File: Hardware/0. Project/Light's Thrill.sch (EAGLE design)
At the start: 26 parts, among them CN6 mini-PCIe board connector, U2 ATMEGA32U4, U3 MT3608, Y1 16MHz

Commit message: WIP
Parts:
- added C2: 10uF, My-RLC:C_0603
- added R2, R3: 0R (5%), My-RLC:R_0603
- R8, R9: value 22R -> 22R (5%)
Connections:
- new net N$8: CN6.CLKREQ#, R2.2
- new net P$1: D4.C, R3.2
- net +5V: now also R3.1; no longer D4.C
- net 0V: now also C2.2, R2.1
- net VBUS: now also C2.1
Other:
- moved on the sheet: CN2-1, CN2-2, CN3-1, CN3-2, CN3-3, CN4-1, CN4-2, CN4-3, CN5, D2

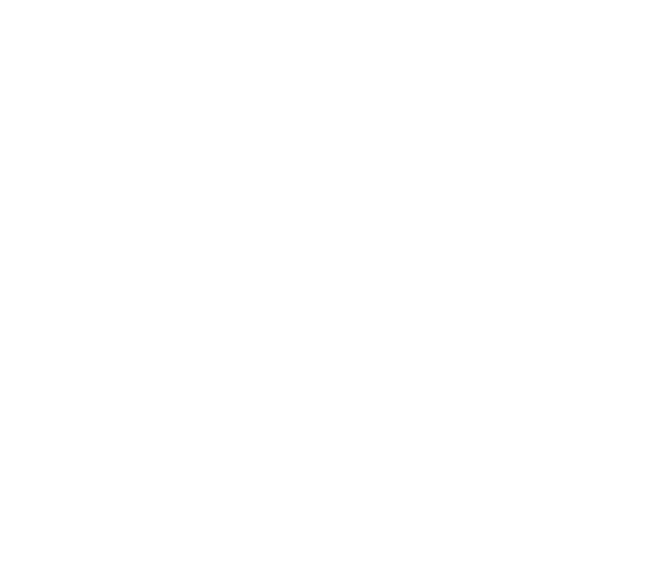
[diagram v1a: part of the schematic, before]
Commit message: HoodLoader + Mega + CLP working properly
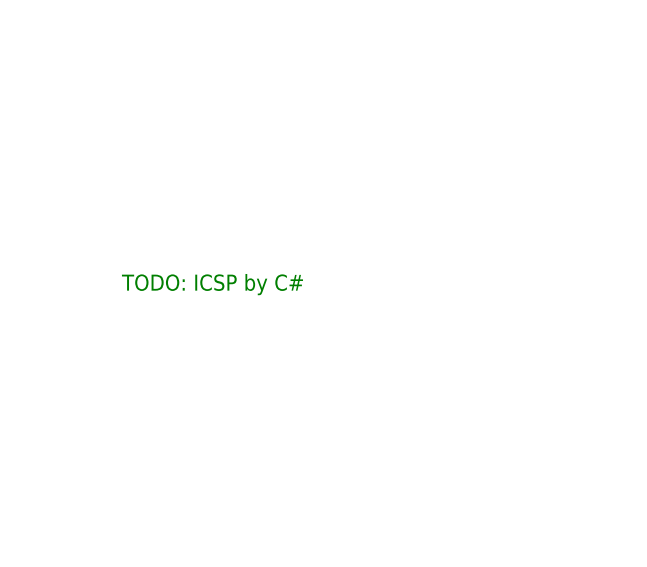
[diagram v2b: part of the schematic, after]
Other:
- note added: "TODO: ICSP by C#"
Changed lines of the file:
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@@
 <setting verticaltext="up"/>
 </settings>
-<grid distance="0.025" unitdist="inch" unit="inch" style="lines" multiple="1" display="no" altdistance="0.01" altunitdist="inch" altunit="inch"/>
+<grid distance="0.1" unitdist="inch" unit="inch" style="lines" multiple="1" display="no" altdistance="0.01" altunitdist="inch" altunit="inch"/>
 <layers>
 <layer number="1" name="Top" color="4" fill="1" visible="no" active="no"/>
@@
 <wire x1="323.215" y1="-160.655" x2="323.215" y2="-43.815" width="0.254" layer="152" style="longdash"/>
 <text x="219.71" y="-48.895" size="2.54" layer="152" ratio="5">BOOST CONVERTER (DC-DC STEP UP)</text>
+<text x="86.36" y="203.2" size="1.778" layer="91">TODO: ICSP by C#</text>
 </plain>
 <instances>
